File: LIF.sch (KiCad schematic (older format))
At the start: 18 parts, among them Q13 2SK3018, U1 AZ4580, U3 74AHC1G08

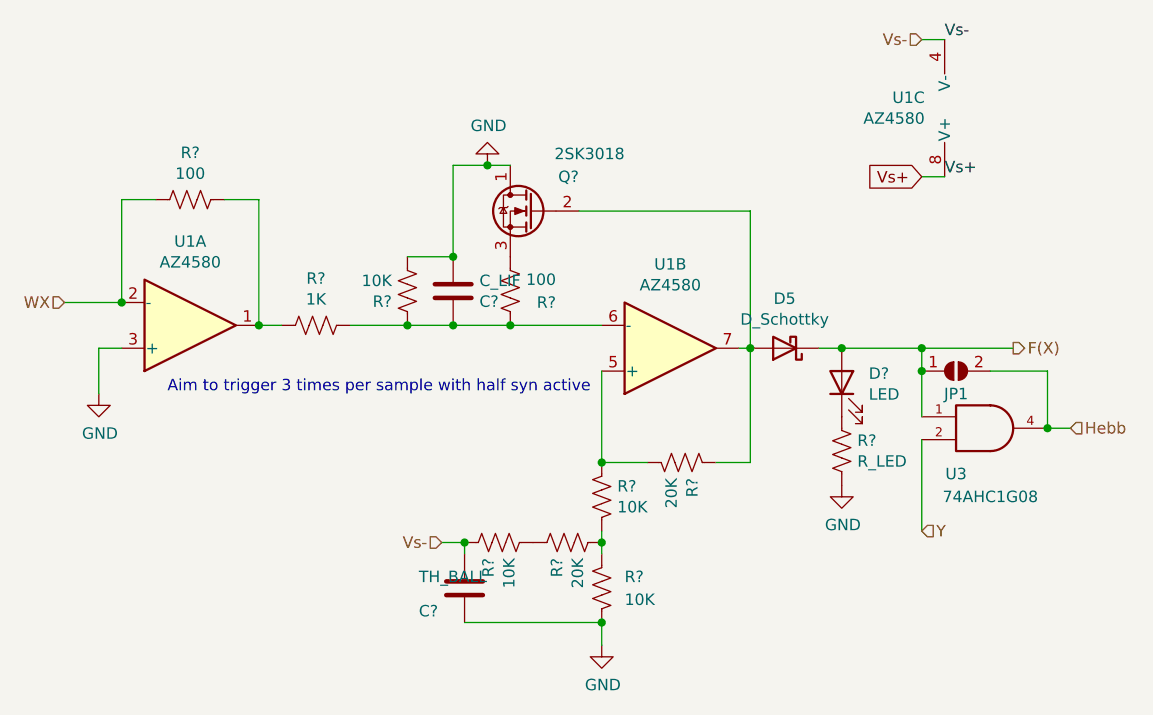
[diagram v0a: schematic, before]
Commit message: Likely Final Component Values
Most values for components that are not dependent on synapse number have been selected.
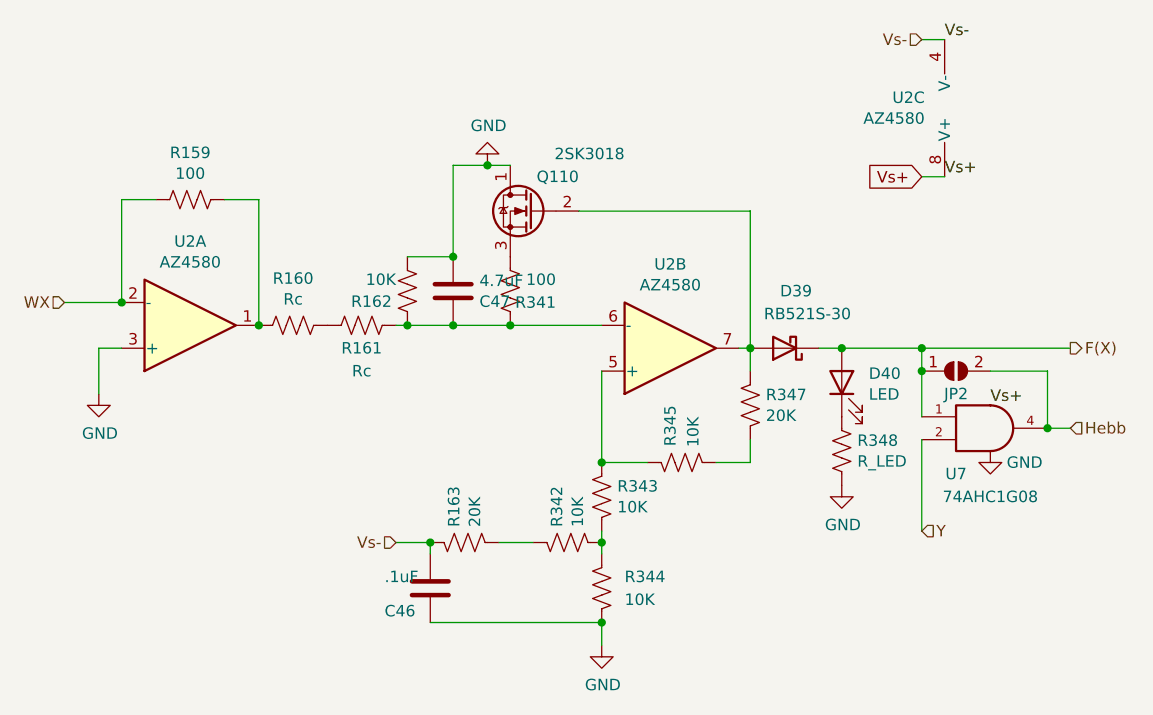
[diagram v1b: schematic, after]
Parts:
- added R156: 10K, Resistor_SMD:R_0603_1608Metric_Pad1.05x0.95mm_HandSolder, symbol Device:R_US
- added R158: 20K, Resistor_SMD:R_0603_1608Metric_Pad1.05x0.95mm_HandSolder, symbol Device:R_US
- C5: value C_LIF -> 4.7uF
- C6: value TH_BALL -> .1uF
- D5: value D_Schottky -> RB521S-30
- R17, R21: Notes (none) -> Set such that Vs/R = 60mA
- R18: value 1K -> Rc; Notes (none) -> Adjust to charge C_LIF to 2.5 in 2.5ms
- R20: value 10K -> 20K
- R22: value 20K -> Rc; Notes (none) -> Adjust to charge C_LIF to 2.5 in 2.5ms
- R25: value 20K -> 10K
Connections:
- net Vs+ is gone; now on net VCC: U1.8 (V+)
- net at R23.2, R24.1: now also R156.2; no longer R22.2
- net at C5.1, R19.2, R21.2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: now also R22.1; no longer R18.1
- net at D5.2 (A), Q13.2 (G), U1.7: now also R158.1; no longer R25.1
- net at R20.2: now also R156.1; no longer R22.1
- new net: R158.2, R25.1
- new net: R18.1, R22.2
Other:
- note removed: "Aim to trigger 3 times per sample with half syn active"
- moved on the sheet: C46, R160, R163
